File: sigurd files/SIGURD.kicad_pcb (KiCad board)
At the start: 2 copper layers, 107 parts, among them J1 jst_sh 4, J10 CAN out (optional), J11 12V/24V Terminal, J2 Hall sensor, J3 12V Terminal, J4 PWM, J5 24V Terminal, J6 Step Up Terminal, J7 Motor Terminal, J8 INPUT, J9 CAN input, Q1 MMBT3904, U1 LMR50410Y5FQDBVRQ1, U2 STM32U575CGTx, U3 VN7050ASTR, U4 VN7050ASTR, U5 VN7050ASTR, U6 AMS1117-3.3, U7 LMV324AIDR, U8 TCAN334GDCN, Y1 48MHz

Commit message: funny fortnite
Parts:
- added D11: LED, LED_SMD:LED_0603_1608Metric_Pad1.05x0.95mm_HandSolder, F.Cu at (155.3, 79.3)
- added R31: 1k, Resistor_SMD:R_0603_1608Metric_Pad0.98x0.95mm_HandSolder, F.Cu at (153.8, 79.3)
- added R33: 47k, Resistor_SMD:R_0603_1608Metric_Pad0.98x0.95mm_HandSolder, F.Cu at (127.5, 141.8)
- R10, R11, R12, R4, R6, R7: footprint Resistor_SMD:R_0201_0603Metric_Pad0.64x0.40mm_HandSolder -> Resistor_SMD:R_0603_1608Metric_Pad0.98x0.95mm_HandSolder
- R27, R28, R32: footprint Resistor_SMD:R_0603_1608Metric -> Resistor_SMD:R_0603_1608Metric_Pad0.98x0.95mm_HandSolder
- moved R16 136.0 mm to (159.0, 151.2)
- moved J3 134.4 mm to (99.5, 159.2)
- moved J5 128.8 mm to (113.0, 159.1)
- moved H4 122.8 mm to (166.5, 151.2)
- moved H3 122.8 mm to (187.7, 49.3)
- moved D1 122.4 mm to (100.0, 147.7), turned to 90 degrees
- moved F6 120.1 mm to (104.5, 146.3), turned to 90 degrees
- moved D3 117.6 mm to (128.0, 147.8), turned to 90 degrees
- moved J11 116.1 mm to (127.0, 158.8)
- moved D4 114.9 mm to (115.5, 147.4), turned to -90 degrees
- moved R17 114.1 mm to (187.6, 57.0), turned to 90 degrees
- moved F7 113.0 mm to (118.5, 146.3), turned to 90 degrees
- moved D6 112.5 mm to (129.5, 147.8), turned to -90 degrees
- moved D7 111.9 mm to (101.5, 147.7), turned to -90 degrees
- moved R27 108.9 mm to (98.5, 147.7), turned to 90 degrees
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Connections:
- D3 pad 2: JMPR -> Net-(D3-A)
- F2 pad 2: Net-(J6-Pin_3) -> Net-(J6-Pin_2)
- J6 pad 2: VCC -> Net-(J6-Pin_2)
- J6 pad 3: Net-(J6-Pin_3) -> VCC
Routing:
- net 5V: track 0.00 -> 4.23 mm
- net +3V3: track 0.00 -> 3.54 mm

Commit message: big chungus wholesome 100
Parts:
- removed JP1: SolderJumper_2_Open, Jumper:SolderJumper-2_P1.3mm_Open_TrianglePad1.0x1.5mm
- removed R19: 120, Resistor_SMD:R_0603_1608Metric_Pad0.98x0.95mm_HandSolder
- added JP3: SolderJumper_2_Open, Jumper:SolderJumper-2_P1.3mm_Open_TrianglePad1.0x1.5mm, F.Cu at (108.5, 67.0)
- added R34: 120, Resistor_SMD:R_0603_1608Metric_Pad0.98x0.95mm_HandSolder, F.Cu at (108.5, 65.0)
- moved R18 115.0 mm to (166.5, 142.5), turned to -90 degrees
- moved R16 108.2 mm to (51.0, 144.4), turned to -90 degrees
- moved R6 53.8 mm to (84.5, 105.4)
- moved D11 46.8 mm to (108.6, 76.5), turned to -90 degrees
- moved J7 45.8 mm to (61.8, 116.0)
- moved J2 45.8 mm to (63.5, 100.0)
- moved J4 45.4 mm to (60.6, 128.5)
- moved R37 45.0 mm to (83.0, 108.8), turned to 90 degrees
- moved R31 43.8 mm to (110.1, 76.5), turned to -90 degrees
- moved C3 43.0 mm to (72.1, 103.0)
- moved R7 42.7 mm to (73.0, 106.3)
- moved R12 42.1 mm to (71.5, 99.0), turned to 90 degrees
- moved R36 41.9 mm to (70.0, 106.3)
- moved U7 41.6 mm to (78.0, 103.0)
- moved R4 41.3 mm to (83.0, 105.4)
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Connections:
- J2 pad 1: /pull_3 -> /pull_1
- J2 pad 3: /pull_1 -> /pull_3
- R10 pad 1: /pull_3 -> /pull_1
- R35 pad 2: /pull_3 -> /pull_1
- R37 pad 2: /pull_1 -> /pull_3
- R4 pad 1: /pull_1 -> /pull_3
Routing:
- net /CAN_H: track 0.00 -> 23.7 mm
- net /CAN_L: track 0.00 -> 23.5 mm, vias 0 -> 1
- net 5V: track 4.23 -> 0.00 mm
- net +3V3: track 3.54 -> 0.12 mm
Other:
- copper layers 2 -> 4

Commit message: Liugma
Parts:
- moved R34 8.83 mm to (100.2, 62.0), turned to -90 degrees
- moved D8 7.35 mm to (108.0, 68.1)
- moved U8 6.52 mm to (108.0, 62.5), turned to 90 degrees
- moved JP3 5.50 mm to (103.0, 66.8), turned to 180 degrees
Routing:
- net /CAN_L: track 23.5 -> 35.5 mm
- net /CAN_H: track 23.7 -> 35.4 mm, vias 0 -> 2
- net Earth: track 0.09 -> 8.58 mm, vias 0 -> 5
- net Net-(JP3-B): track 0.00 -> 4.75 mm
- net /CAN_TX: track 0.00 -> 4.27 mm
- net /CAN_RX: track 0.00 -> 4.25 mm
- net +3V3: track 0.12 -> 1.87 mm, vias 0 -> 1
- added copper zone on In2.Cu, net +24V
- added copper zone on F.Cu, net +3V3
- added copper zone on In1.Cu, net 5V
- added copper zone on B.Cu, net Earth

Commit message: Goober
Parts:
- removed CR1: 1N4448, 1N4448:SOD27_NEX
- added D12: D, Diode_SMD:D_SOD-523, F.Cu at (77.9, 80.9)
- F1: value 1.5A -> 1.0A
- F6, F7, F8: value Polyfuse -> 2.0 A
- moved C12 45.3 mm to (129.4, 125.1), turned to 180 degrees
- moved C10 44.7 mm to (135.5, 114.5), turned to 90 degrees
- moved R12 43.2 mm to (113.2, 110.6)
- moved R35 42.2 mm to (111.5, 106.9), turned to -90 degrees
- moved J7 41.9 mm to (97.1, 138.7)
- moved R13 41.5 mm to (147.0, 132.2), turned to -90 degrees
- moved R10 40.2 mm to (111.5, 110.6)
- moved J3 39.3 mm to (138.4, 153.6)
- moved D1 39.3 mm to (138.9, 142.1)
- moved D5 39.3 mm to (134.9, 142.2)
- moved D7 39.3 mm to (140.4, 142.1)
- moved F6 39.3 mm to (143.4, 140.7)
- moved R27 39.3 mm to (137.4, 142.1)
- moved R29 39.3 mm to (138.9, 137.3)
- moved U5 39.3 mm to (142.8, 132.9)
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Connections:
- net Net-(J8-Pin_2) renamed V_input
- net VCC renamed +10V
- U2 pad 17: /MOTOR -> unconnected-(U2-PA7-Pad17)
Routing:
- net Earth: track 8.58 -> 130.2 mm, vias 5 -> 29
- net /SOL3_SENSE: track 0.00 -> 34.6 mm
- net +3V3: track 1.87 -> 35.5 mm, vias 1 -> 2
- net /SOL2_SENSE: track 0.00 -> 22.0 mm, vias 0 -> 2
- net /pull_1: track 0.00 -> 21.3 mm, vias 0 -> 2
- net /pull_2: track 0.00 -> 20.6 mm, vias 0 -> 2
- net 5V: track 0.00 -> 19.7 mm, vias 0 -> 5
- net /HALL3_buff: track 0.00 -> 19.0 mm
- net /HALL2_buff: track 0.00 -> 18.6 mm
- net /OSC_IN: track 0.00 -> 15.4 mm
- net /NRST: track 0.00 -> 15.4 mm, vias 0 -> 2
- net +10V: track 0.00 -> 12.9 mm
- net /pull_3: track 0.00 -> 12.2 mm
- net /LED_R: track 0.00 -> 12.2 mm
- net /OSC_OUT: track 0.00 -> 11.7 mm
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- added copper zone on F.Cu, net +10V
- added copper zone on F.Cu, net /SOL1_OUT
- added copper zone on F.Cu, net /SOL2_OUT
- added copper zone on F.Cu, net /SOL3_OUT
- added copper zone on F.Cu, net Earth
- removed copper zone on In1.Cu, net 5V

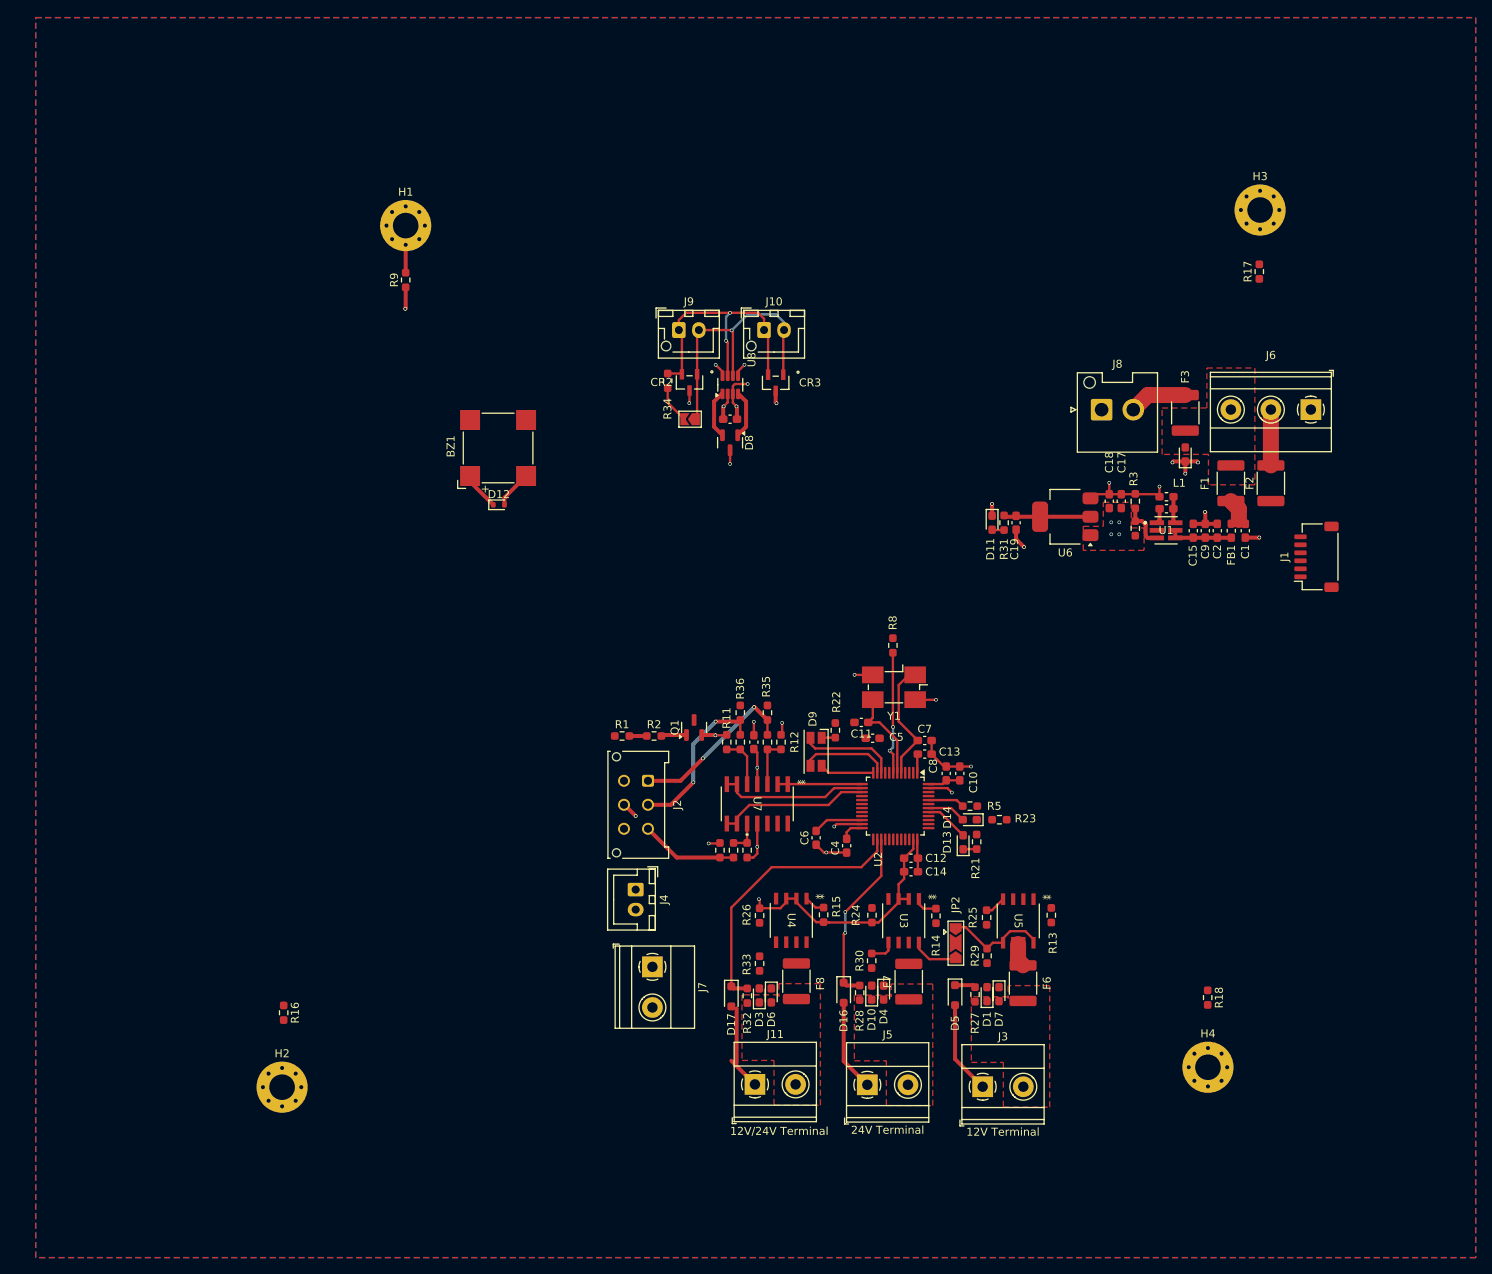
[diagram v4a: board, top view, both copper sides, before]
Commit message: Everything but power traces routed
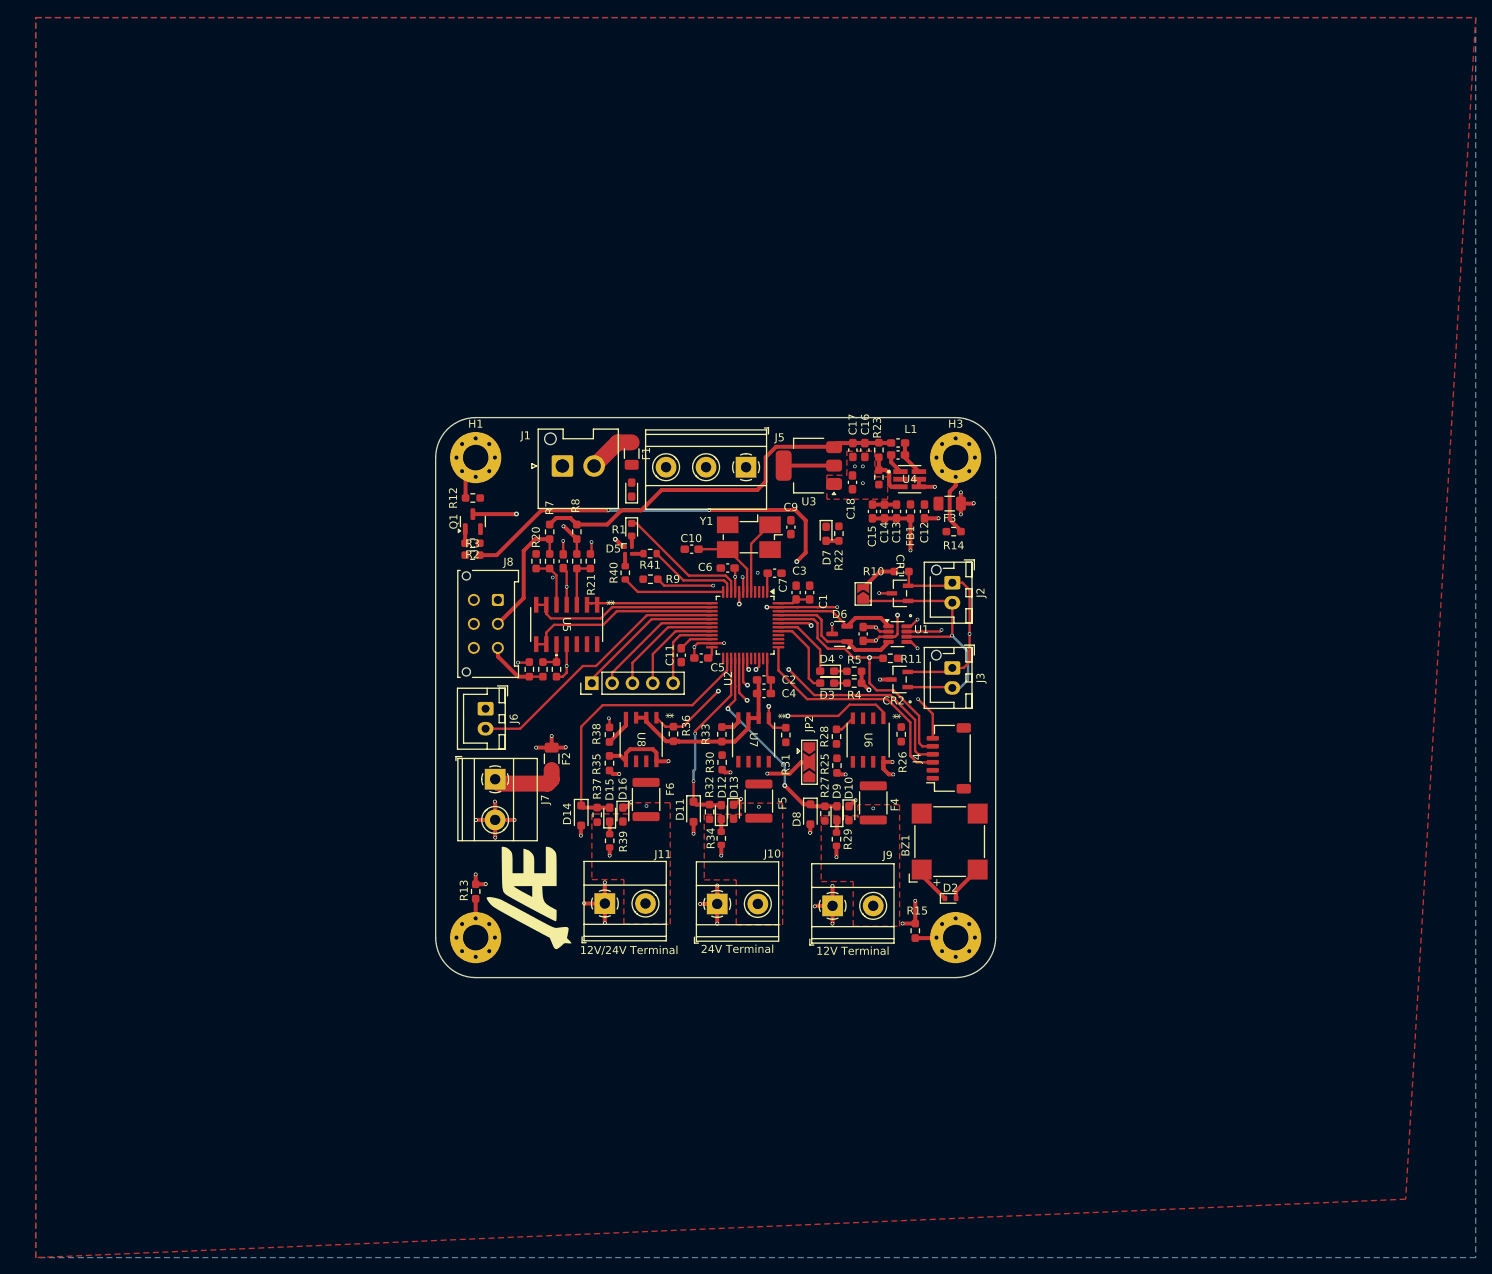
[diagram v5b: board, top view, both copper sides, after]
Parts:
- removed the D10 at (124.5, 141.9)
- removed the D3 at (110.5, 142.2)
- removed the D9 at (117.6, 111.8)
- removed the F1 at (169.4, 78.2)
- removed F7, F8: 2.0 A, Fuse:Fuse_1812_4532Metric_Pad1.30x3.40mm_HandSolder
- removed the R22 at (120.0, 109.1)
- added D12: LED, LED_SMD:LED_0603_1608Metric_Pad1.05x0.95mm_HandSolder, F.Cu at (105.7, 119.3)
- added D15: LED, LED_SMD:LED_0603_1608Metric_Pad1.05x0.95mm_HandSolder, F.Cu at (91.8, 119.6)
- added D5: LED_ARBG, LED_SMD:LED_Lumex_SML-LX0404SIUPGUSB, F.Cu at (94.1, 86.6)
- added F3: Fuse, Fuse:Fuse_1206_3216Metric, F.Cu at (134.2, 80.8)
- added F4: 2.0 A, Fuse:Fuse_1812_4532Metric, F.Cu at (124.7, 118.2)
- added F5: 2.0 A, Fuse:Fuse_1812_4532Metric, F.Cu at (110.4, 117.9)
- added G***: LOGO, AESIR LOGO:AESIR LOGO, F.Cu at (81.9, 130.0)
- added J12: Extra NF, Connector_PinHeader_2.54mm:PinHeader_1x05_P2.54mm_Vertical, F.Cu at (89.5, 103.2)
- added R1: 56, LED_SMD:LED_0603_1608Metric, F.Cu at (94.5, 84.0)
- added R29: 100, Resistor_SMD:R_0603_1608Metric, F.Cu at (120.1, 122.7)
- added R34: 100, Resistor_SMD:R_0603_1608Metric, F.Cu at (105.7, 122.6)
- added R39: 100, Resistor_SMD:R_0603_1608Metric, F.Cu at (91.8, 122.9)
- added R40: 22, Resistor_SMD:R_0603_1608Metric, F.Cu at (93.7, 89.4)
- added R41: 56, Resistor_SMD:R_0603_1608Metric, F.Cu at (96.8, 87.0)
- F1: renamed from F3; footprint Fuse:Fuse_1812_4532Metric_Pad1.30x3.40mm_HandSolder -> Fuse:Fuse_1206_3216Metric
- F2: value 4A -> 5A; footprint Fuse:Fuse_1812_4532Metric_Pad1.30x3.40mm_HandSolder -> Fuse:Fuse_1206_3216Metric
- F6: footprint Fuse:Fuse_1812_4532Metric_Pad1.30x3.40mm_HandSolder -> Fuse:Fuse_1812_4532Metric
- R4: renamed from R21; value 470 -> ~
- R5: renamed from R23; value 470 -> ~
- moved F2 96.3 mm to (84.5, 112.7), turned to -90 degrees
- moved BZ1 74.9 mm to (134.2, 123.0)
- moved D2 74.9 mm to (134.3, 130.1)
- moved J5 71.0 mm to (108.8, 76.2)
- moved F1 69.4 mm to (94.5, 74.5)
- moved D1 69.3 mm to (94.5, 79.0)
- moved J1 67.8 mm to (85.8, 76.0)
- moved J4 52.4 mm to (134.1, 112.6)
- moved F6 52.4 mm to (96.3, 117.7)
- moved R14 50.2 mm to (134.8, 84.2), turned to 0 degrees
- moved H3 49.0 mm to (135.0, 75.0)
- moved J3 48.3 mm to (134.6, 101.3), turned to -90 degrees
- moved J2 46.5 mm to (134.6, 90.6), turned to -90 degrees
- moved CR2 40.2 mm to (128.0, 102.7), turned to 90 degrees
- moved C12 40.2 mm to (131.1, 81.7)
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- renumbered C10 to C1, C11 to C10, C6 to C11, C1 to C12, C2 to C13, C9 to C14, C17 to C16, C18 to C17, C19 to C18, C16 to C19, C12 to C2, C3 to C20, C13 to C3, C14 to C4, C4 to C5, C5 to C6, C8 to C7, C20 to C8, C7 to C9, CR2 to CR1, CR3 to CR2, D2 to D1, D7 to D10, D16 to D11, D4 to D13, D17 to D14, D6 to D16, D12 to D2, D13 to D3, D14 to D4, D8 to D6, D11 to D7, D5 to D8, D1 to D9, J8 to J1, J5 to J10, J9 to J2, J10 to J3, J1 to J4, J6 to J5, J4 to J6, J2 to J8, J3 to J9, JP3 to JP1, R34 to R10, R5 to R11, R9 to R12, R16 to R13, R17 to R14, R18 to R15, R4 to R16, R7 to R17, R10 to R18, R6 to R19, R11 to R20, R12 to R21, R31 to R22, R3 to R23, R20 to R24, R29 to R25, R13 to R26, R25 to R28, R1 to R3, R14 to R31, R28 to R32, R24 to R33, R33 to R35, R15 to R36, R32 to R37, R26 to R38, R37 to R6, R36 to R7, R35 to R8, R8 to R9, U8 to U1, U6 to U3, U1 to U4, U7 to U5, U5 to U6, U3 to U7, U4 to U8
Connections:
- D9 pad 1: /SOL1_OUT -> Net-(D9-K)
- D9 pad 2: Net-(D1-A) -> /SOL1_SENSE
- F2 pad 2: Net-(J6-Pin_2) -> Net-(J7-Pin_1)
- F6 pad 1: /SOL1_OUT -> /SOL3_OUT
- J5 pad 2: Net-(J6-Pin_2) -> +24V
- J7 pad 1: +24V -> Net-(J7-Pin_1)
- R25 pad 2: Net-(D1-A) -> /SOL1_OUT
- R30 pad 2: Net-(D10-A) -> /SOL2_OUT
- R35 pad 2: Net-(D3-A) -> /SOL3_OUT
- U2 pad 11: /LED_G -> /LED_B
- U2 pad 12: /LED_B -> /LED_G
- U2 pad 17: unconnected-(U2-PA7-Pad17) -> /PA7
- U2 pad 18: unconnected-(U2-PB0-Pad18) -> /PB0
- U2 pad 19: unconnected-(U2-PB1-Pad19) -> /PB1
- U2 pad 20: unconnected-(U2-PB2-Pad20) -> /PB2
- U2 pad 21: unconnected-(U2-PB10-Pad21) -> /PB10
- U6 pad 6: Net-(F6-Pad2) -> Net-(F4-Pad2)
- U6 pad 7: Net-(F6-Pad2) -> Net-(F4-Pad2)
- U8 pad 6: Net-(F8-Pad2) -> Net-(F6-Pad2)
- U8 pad 7: Net-(F8-Pad2) -> Net-(F6-Pad2)
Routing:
- net /BUZZER: track 2.17 -> 62.2 mm, vias 0 -> 4
- net 5V: track 19.7 -> 55.4 mm, vias 5 -> 2
- net /MOTOR_PWM: track 0.00 -> 34.2 mm
- net /NRST: track 15.4 -> 48.5 mm, vias 2 -> 4
- net /SW_DIO: track 0.00 -> 30.3 mm, vias 0 -> 2
- net /SW_CLK: track 0.00 -> 29.4 mm
- net JMPR: track 0.00 -> 29.0 mm, vias 0 -> 2
- net /BOOT0: track 4.57 -> 32.6 mm, vias 0 -> 1
- net /SOL1: track 0.00 -> 25.2 mm, vias 0 -> 2
- net /SOL1_SENSE: track 2.60 -> 26.8 mm, vias 0 -> 2
- net /PA7: track 0.00 -> 18.6 mm
- net /PB0: track 0.00 -> 16.3 mm
- net /PB1: track 0.00 -> 14.3 mm
- net /SOL3: track 2.59 -> 16.4 mm, vias 0 -> 2
- net Earth: track 130.2 -> 116.6 mm, vias 29 -> 46
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- added copper zone on In1.Cu, net +10V
- removed copper zone on F.Cu, net +10V
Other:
- board outline added: 70 x 70 mm

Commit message: Almost complete board
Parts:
- moved D2 0.80 mm to (134.3, 129.3)
- moved JP2 0.19 mm to (116.7, 112.9)
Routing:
- net Net-(BZ1-+): track 10.2 -> 129.8 mm, vias 1 -> 5
- net Earth: track 116.6 -> 187.2 mm, vias 46 -> 63
- net +3V3: track 38.4 -> 61.6 mm, vias 5 -> 7
- net V_input: track 5.92 -> 0.00 mm, vias 0 -> 4
- net +24V: track 5.17 -> 8.06 mm, vias 3 -> 8
- net /OSC_IN: track 9.37 -> 12.2 mm
- net +10V: track 7.91 -> 9.88 mm
- net Net-(F5-Pad2): track 0.00 -> 1.27 mm
- net JMPR: track 29.0 -> 27.7 mm
- net /pull_1: track 16.8 -> 17.9 mm
- net /SOL3_SENSE: track 36.2 -> 37.2 mm
- added copper zone on B.Cu, net +10V
- added copper zone on F.Cu, net +10V
- added copper zone on In2.Cu, net +10V
- added copper zone on F.Cu, net +24V
- added copper zone on In1.Cu, net +24V
- added copper zone on F.Cu, net Net-(F5-Pad2)
- added copper zone on B.Cu, net V_input
- added copper zone on F.Cu, net V_input
- added copper zone on In1.Cu, net V_input
- added copper zone on In2.Cu, net V_input
- removed copper zone on In2.Cu, net +24V
